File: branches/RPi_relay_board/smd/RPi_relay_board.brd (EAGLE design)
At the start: 75.9 x 61.6 mm, 44 parts, among them K1 351, K2 351, T1 ZXTN2020F, T2 ZXTN2020F, T3 ZXTN2020F, U1 MAX232SOIC16

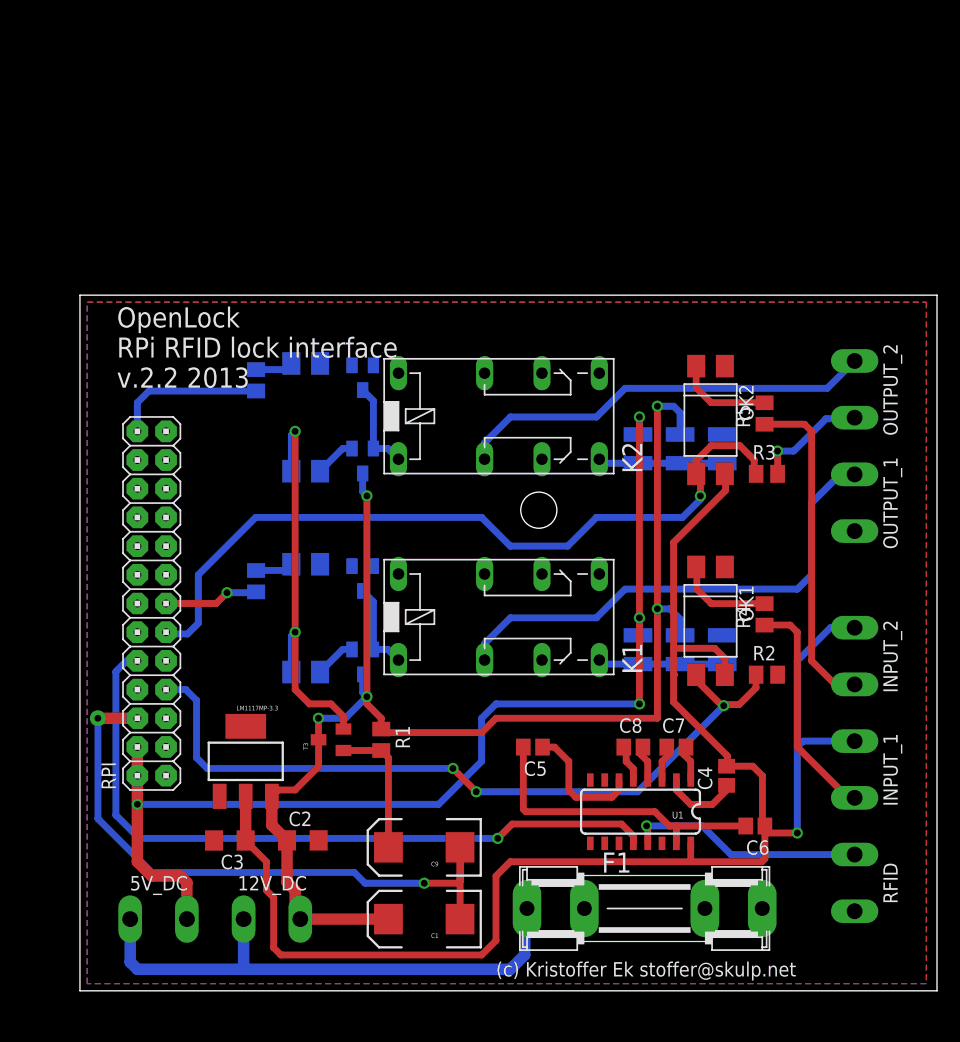
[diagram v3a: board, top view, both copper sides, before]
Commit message: smaller pcb, so it fits in RS 458-0768
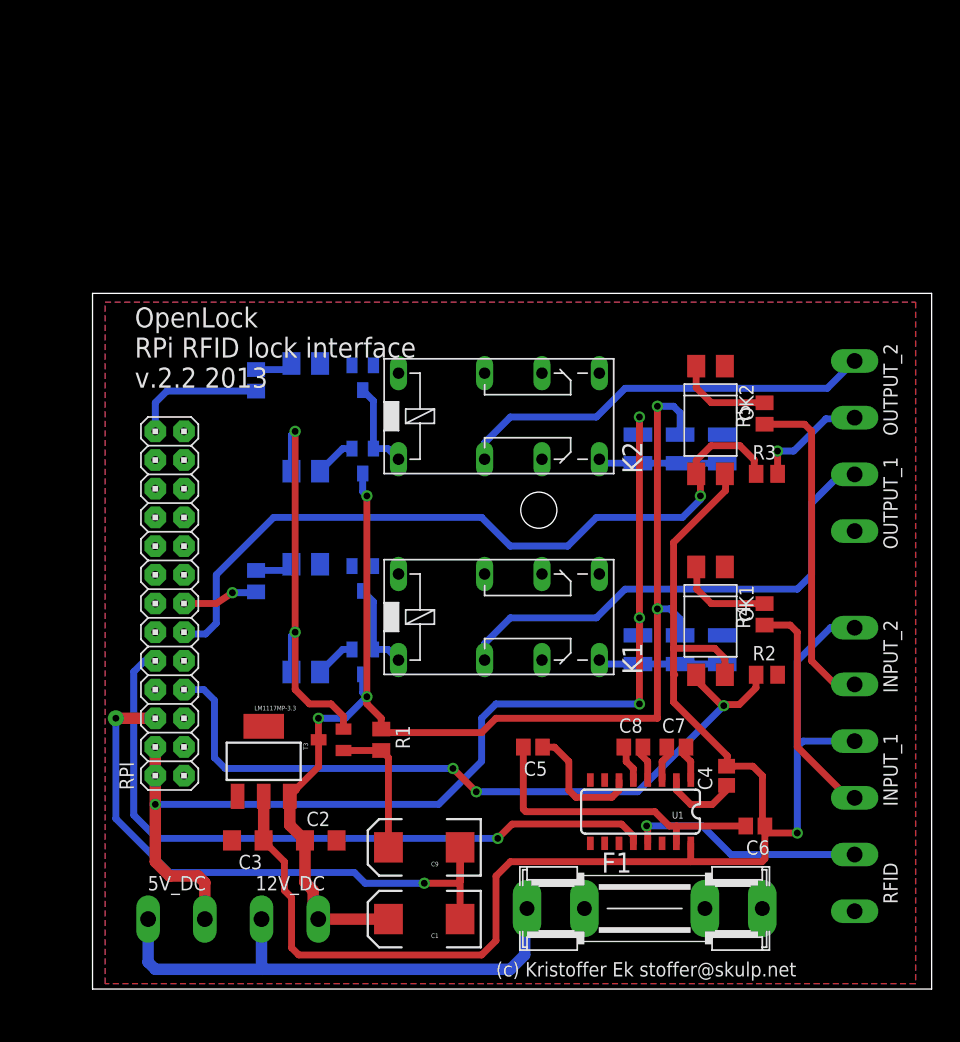
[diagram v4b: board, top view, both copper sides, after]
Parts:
- moved C3 1.59 mm to (23.7, 6.96)
- moved LM1117MP-3.3 1.59 mm to (25.2, 14.0)
- moved RPI 1.59 mm to (16.8, 27.9)
- moved 12V_DC 1.59 mm to (25.0, 0.00)
- moved 5V_DC 1.59 mm to (14.9, 0.00)
- moved C2 1.59 mm to (30.2, 6.96)
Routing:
- net +12V: track 120.8 -> 117.8 mm
- net N$44: track 8.39 -> 6.70 mm
- net N$4: track 68.1 -> 66.5 mm
- net N$15: track 63.3 -> 61.7 mm
- net +5V: track 97.6 -> 96.0 mm
- net N$6: track 13.5 -> 11.9 mm
- net N$17: track 48.2 -> 46.6 mm
- net N$1: track 68.0 -> 66.4 mm
- net GND: track 93.6 -> 92.1 mm
- net 3.3V: track 143.7 -> 142.1 mm
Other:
- board size 75.9 x 61.6 mm -> 74.3 x 61.6 mm
